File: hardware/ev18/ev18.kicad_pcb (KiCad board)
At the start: 4 copper layers, 112.3 x 90 mm, 234 parts, among them CN1 Conn_05x02_Female, CN2 PJ-242, J1 USB_C_Receptacle, J11 Conn_02x05_Counter_Clockwise, J2 Conn_01x02_Socket, J3 AudioJack4, J4 Conn_02x03_Odd_Even, J5 Conn_02x03_Odd_Even, J6 Conn_02x05_Counter_Clockwise, J7 Conn_02x05_Counter_Clockwise, J8 Conn_02x05_Counter_Clockwise, J9 Conn_02x05_Counter_Clockwise, Q1 2N7002, Q2 2N7002, Q3 2N7002, SW1 SW_SPDT, SW2 SW_Push, SW3 SW_Push, SW4 SW_Push, SW5 SW_Push, SW6 SW_Push, SW7 SW_Push, U1 BQ21040DBV, U10 STM32F405RGTx, U12 XC6227C301MR-G, U2 USBLC6-2P6, U3 STM32F072CBTx, U4 CH340C, U5 TPS63060, U6 WM8960CGEFL/RV, U7 ESP32-S3-WROOM-1, U8 M24C02-RMN6TP, U9 TPS2116DRL, Y1 Crystal_GND24

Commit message: address PR review
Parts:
- removed NT4: NetTie_2, NetTie:NetTie-2_SMD_Pad0.5mm
- TP31: moved to B.Cu
- moved TP31 42.4 mm to (74.4, 95.0), turned to 180 degrees
- moved R65 29.5 mm to (70.8, 95.9), turned to 90 degrees
- moved TP28 5.22 mm to (60.7, 42.8)
- moved TP3 1.10 mm to (64.1, 22.7)
- moved R11 0.62 mm to (72.1, 96.4)
- moved SW2 0.61 mm to (74.4, 95.0)
- moved R6 0.39 mm to (73.0, 98.8)
- moved R47 0.07 mm to (69.5, 96.4)
- moved C12 0.06 mm to (66.1, 102.1)
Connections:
- C12 pad 1: Net-(J2-Pin_2) -> /BQ_OUT
- R11 pad 1: Net-(J2-Pin_2) -> /BQ_OUT
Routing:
- net GNDA: track 118.4 -> 145.8 mm, vias 31 -> 36
- net Net-(J2-Pin_2): track 100.6 -> 89.0 mm, vias 6 -> 5
- net /BQ_OUT: track 1.47 -> 12.9 mm, vias 5 -> 7
- net VBUS: track 46.1 -> 49.7 mm
- net /MIC_N: track 23.2 -> 24.5 mm
- net Net-(D3-BK): track 19.6 -> 20.2 mm
- net VSYS: track 108.5 -> 109.0 mm
- net +3.0VA: track 12.9 -> 13.4 mm
- net Net-(D1-K): track 25.0 -> 24.4 mm
- net Net-(D1-A): track 3.91 -> 4.43 mm

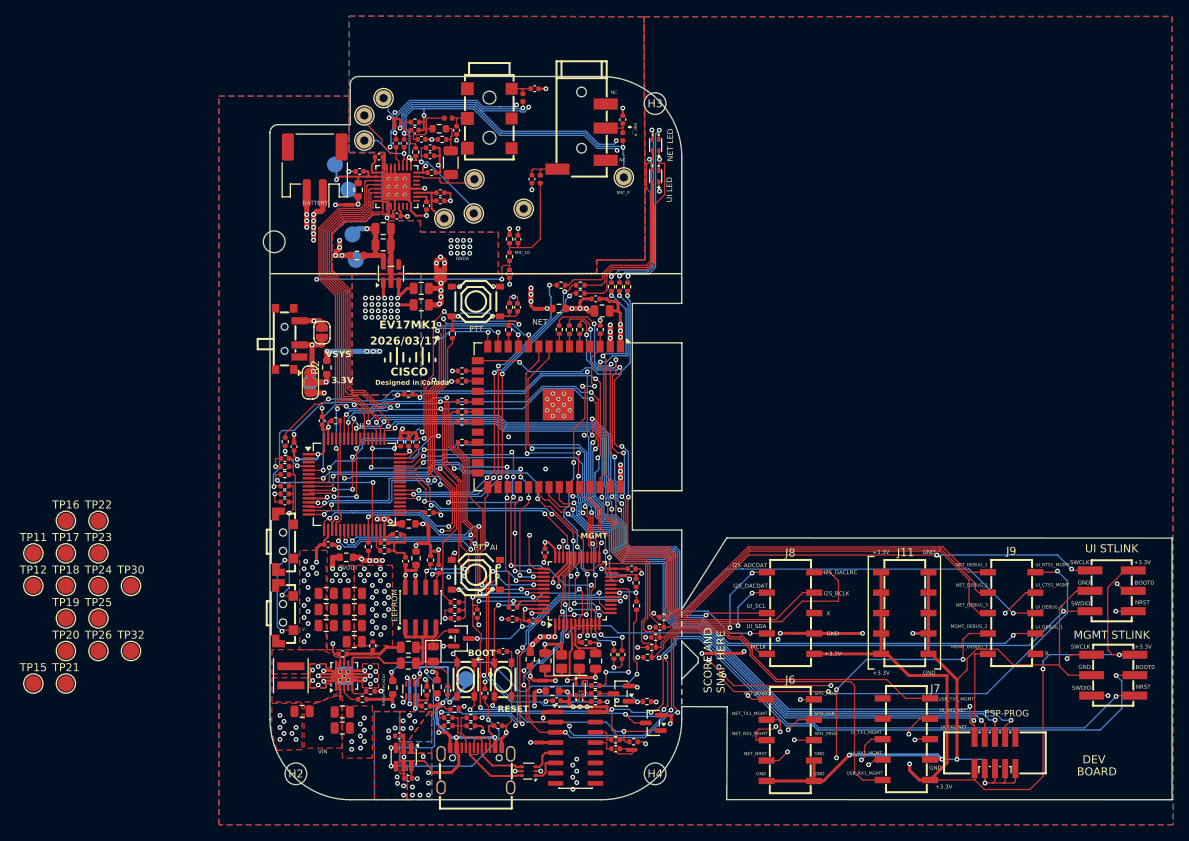
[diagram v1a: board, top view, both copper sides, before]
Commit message: Update side buttons, 3.5mm jack, and 2.5mm jack footprints to match their datasheets
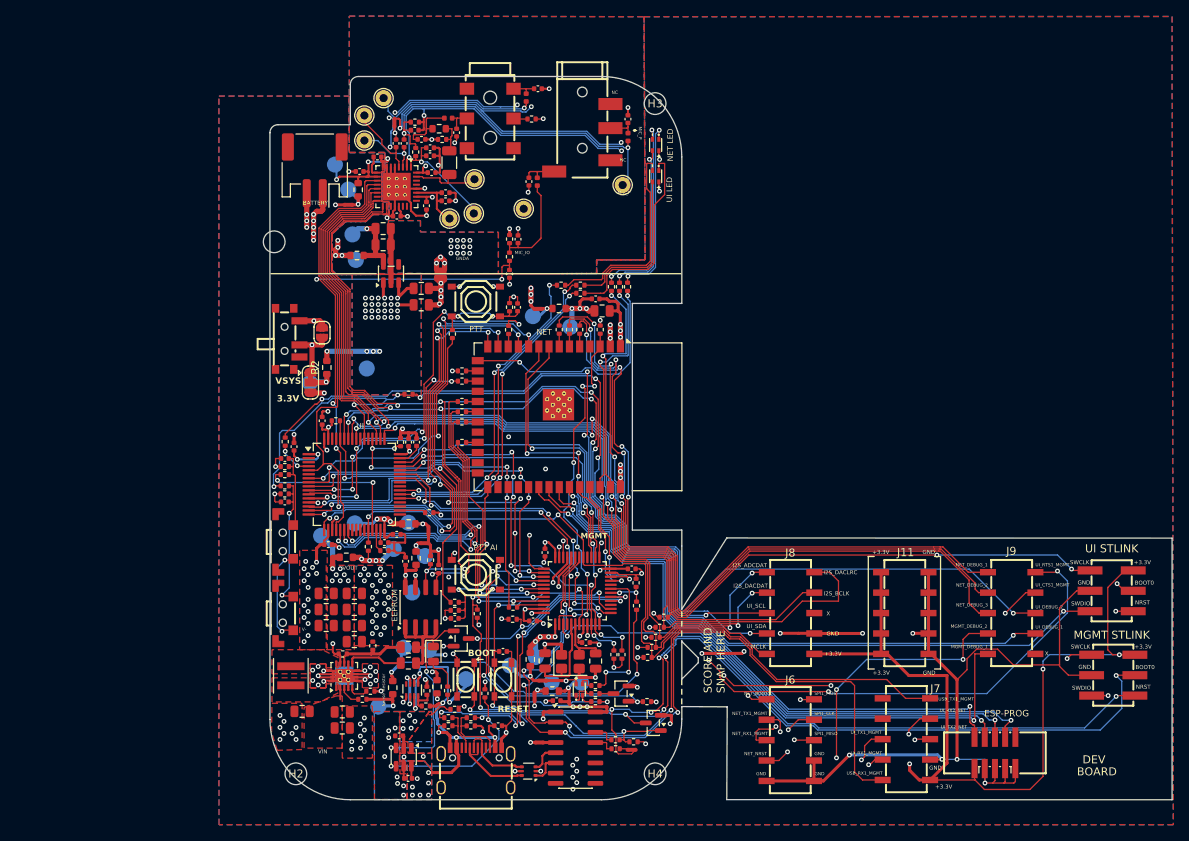
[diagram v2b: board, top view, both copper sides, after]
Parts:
- added R84: 1k0, Resistor_SMD:R_0402_1005Metric, F.Cu at (82.6, 25.3)
- TP11, TP12, TP15, TP16, TP17, TP18, TP19, TP20, TP21, TP22, TP23, TP24, TP25, TP26, TP30, TP32: moved to B.Cu
- moved TP17 68.8 mm to (87.4, 51.2), turned to 180 degrees
- moved TP18 67.1 mm to (82.7, 49.8), turned to 180 degrees
- moved TP21 64.1 mm to (88.7, 95.5), turned to 180 degrees
- moved TP22 59.9 mm to (85.1, 95.4), turned to 180 degrees
- moved TP19 58.7 mm to (83.1, 92.2), turned to 180 degrees
- moved TP20 55.3 mm to (79.9, 93.3), turned to 180 degrees
- moved TP11 48.8 mm to (69.3, 79.7), turned to 180 degrees
- moved TP12 47.2 mm to (67.7, 84.2), turned to 180 degrees
- moved TP15 44.7 mm to (60.6, 75.6), turned to 180 degrees
- moved TP16 42.6 mm to (67.2, 75.5), turned to 180 degrees
- moved TP30 39.9 mm to (62.0, 56.3), turned to 180 degrees
- moved TP25 38.2 mm to (66.6, 91.1), turned to 180 degrees
- moved TP32 37.1 mm to (69.8, 91.4), turned to 180 degrees
- moved TP24 37.0 mm to (65.4, 78.8), turned to 180 degrees
- moved TP26 35.5 mm to (63.5, 98.4), turned to 180 degrees
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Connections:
- CN2 pad 4: unconnected-(CN2-Pad4) -> Net-(CN2-Pad4)
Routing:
- net /MCLK: track 132.3 -> 127.0 mm, vias 5 -> 2
- net +3.3V_WM8960: track 10.5 -> 15.7 mm, vias 1 -> 3
- net /VOLUME-: track 30.4 -> 35.5 mm
- net Net-(J2-Pin_2): track 89.0 -> 93.8 mm, vias 5 -> 6
- net /BB_Vout: track 26.0 -> 30.7 mm
- net +3.3V: track 189.0 -> 192.5 mm, vias 28 -> 27
- net /MGMT_Sense: track 2.58 -> 5.64 mm
- net +3.3V_CH340C: track 15.1 -> 17.7 mm
- net +3.3V_EEPROM: track 4.93 -> 7.42 mm
- net +3.3V_Net: track 8.84 -> 11.2 mm
- net +3.3V_UI: track 26.2 -> 28.5 mm, vias 10 -> 11
- net GNDA: track 145.8 -> 148.1 mm, vias 36 -> 37
- net /CH340C_Sense: track 1.46 -> 3.76 mm
- net +3.3V_Mgmt: track 19.8 -> 22.0 mm
- net VSYS: track 109.0 -> 111.2 mm
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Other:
- board text added: "BB VOUT +"
- board text added: "BB VOUT -"
- board text added: "EV18"
- board text removed: "EV17MK1"

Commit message: Fixed ERC errors and warnings, and fixed update pcb warnings
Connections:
- U3 pad 32: /MGMT_UD_N -> unconnected-(U3-PA11-Pad32)
- U3 pad 33: /MGMT_UD_P -> unconnected-(U3-PA12-Pad33)
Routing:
- net unconnected-(U3-PA11-Pad32): track 0.00 -> 4.28 mm, vias 0 -> 1
- net /MGMT_UD_N: track 4.28 -> 0.00 mm, vias 1 -> 0
- net unconnected-(U3-PA12-Pad33): track 0.00 -> 3.86 mm, vias 0 -> 1
- net /MGMT_UD_P: track 3.86 -> 0.00 mm, vias 1 -> 0
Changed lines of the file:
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@@
 	(net 214 "/CH340C_Sense")
 	(net 215 "/MGMT_Sense")
-	(net 216 "/MGMT_UD_N")
-	(net 217 "/MGMT_UD_P")
+	(net 216 "unconnected-(U3-PA11-Pad32)")
+	(net 217 "unconnected-(U3-PA12-Pad33)")
 	(net 218 "/Jack_HP_L")
 	(net 219 "/Jack_MIC_N")
@@
 			(layers "F.Cu" "F.Mask" "F.Paste")
 			(roundrect_rratio 0.25)
-			(net 216 "/MGMT_UD_N")
+			(net 216 "unconnected-(U3-PA11-Pad32)")
 			(pinfunction "PA11")
-			(pintype "bidirectional")
+			(pintype "bidirectional+no_connect")
 		)
 		(pad "33" smd roundrect
@@
 			(layers "F.Cu" "F.Mask" "F.Paste")
 			(roundrect_rratio 0.25)
-			(net 217 "/MGMT_UD_P")
+			(net 217 "unconnected-(U3-PA12-Pad33)")
 			(pinfunction "PA12")
-			(pintype "bidirectional")
+			(pintype "bidirectional+no_connect")
 		)
 		(pad "34" smd roundrect
@@
 			)
 		)
+		(pad "" smd rect
+			(at -3.8 -0.78 90)
+			(size 1.1 0.93)
+			(layers "F.Cu" "F.Mask" "F.Paste")
+		)
+		(pad "" smd rect
+			(at -3.8 1.49 270)
+			(size 1.1 0.93)
+			(layers "F.Cu" "F.Mask" "F.Paste")
+		)
 		(pad "" np_thru_hole circle
 			(at -1.5 0.36 270)
@@
 			(layers "*.Cu" "*.Mask")
 		)
+		(pad "" smd rect
+			(at 3.8 -0.78 270)
+			(size 1.1 0.93)
+			(layers "F.Cu" "F.Mask" "F.Paste")
+		)
+		(pad "" smd rect
+			(at 3.8 1.49 270)
+			(size 1.1 0.93)
+			(layers "F.Cu" "F.Mask" "F.Paste")
+		)
 		(pad "1" smd rect
 			(at -2.25 -1.49 270)
@@
 			(pintype "passive+no_connect")
 		)
-		(pad "4" smd rect
-			(at 3.8 -0.78 270)
-			(size 1.1 0.93)
-			(layers "F.Cu" "F.Mask" "F.Paste")
-		)
-		(pad "5" smd rect
-			(at 3.8 1.49 270)
-			(size 1.1 0.93)
-			(layers "F.Cu" "F.Mask" "F.Paste")
-		)
-		(pad "6" smd rect
-			(at -3.8 1.49 270)
-			(size 1.1 0.93)
-			(layers "F.Cu" "F.Mask" "F.Paste")
-		)
-		(pad "7" smd rect
-			(at -3.8 -0.78 90)
-			(size 1.1 0.93)
-			(layers "F.Cu" "F.Mask" "F.Paste")
-		)
 		(embedded_fonts no)
 		(model "${KIPRJMOD}/../kicad_libraries/hactar_models.3dshapes/SW-SMD_MK-12C02-G020.wrl"
@@
 			)
 			(rotate
-				(xyz 0 0 0)
+				(xyz -0 -0 -0)
 			)
 		)
@@
 			(layers "F.Cu" "F.Mask" "F.Paste")
 			(net 7 "/MGMT_NRST")
+			(pinfunction "1")
 			(pintype "passive")
 		)
@@
 			(layers "F.Cu" "F.Mask" "F.Paste")
 			(net 7 "/MGMT_NRST")
+			(pinfunction "2")
 			(pintype "passive")
 		)
@@
 			(layers "F.Cu" "F.Mask" "F.Paste")
 			(net 3 "GND")
+			(pinfunction "3")
 			(pintype "passive")
 		)
@@
 			(layers "F.Cu" "F.Mask" "F.Paste")
 			(net 3 "GND")
+			(pinfunction "4")
 			(pintype "passive")
 		)
@@
 			(layers "F.Cu" "F.Mask" "F.Paste")
 			(net 1 "+3.3V")
+			(pinfunction "1")
 			(pintype "passive")
 		)
@@
 			(layers "F.Cu" "F.Mask" "F.Paste")
 			(net 1 "+3.3V")
+			(pinfunction "2")
 			(pintype "passive")
 		)
@@
 			(layers "F.Cu" "F.Mask" "F.Paste")
 			(net 74 "Net-(C47-Pad1)")
+			(pinfunction "3")
 			(pintype "passive")
 		)
@@
 			(layers "F.Cu" "F.Mask" "F.Paste")
 			(net 74 "Net-(C47-Pad1)")
+			(pinfunction "4")
 			(pintype "passive")
 		)
@@
 			(layers "F.Cu" "F.Mask" "F.Paste")
 			(net 1 "+3.3V")
+			(pinfunction "1")
 			(pintype "passive")
 		)
@@
 			(layers "F.Cu" "F.Mask" "F.Paste")
 			(net 1 "+3.3V")
+			(pinfunction "2")
 			(pintype "passive")
 		)
@@
 			(layers "F.Cu" "F.Mask" "F.Paste")
 			(net 73 "Net-(C46-Pad1)")
+			(pinfunction "3")
 			(pintype "passive")
 		)
@@
 			(layers "F.Cu" "F.Mask" "F.Paste")
 			(net 73 "Net-(C46-Pad1)")
+			(pinfunction "4")
 			(pintype "passive")
 		)
@@
 			)
 		)
+		(pad "" smd roundrect
+			(at -3.35 2.9 180)
+			(size 1.5 3.4)
+			(layers "F.Cu" "F.Mask" "F.Paste")
+			(roundrect_rratio 0.166667)
+		)
+		(pad "" smd roundrect
+			(at 3.35 2.9 180)
+			(size 1.5 3.4)
+			(layers "F.Cu" "F.Mask" "F.Paste")
+			(roundrect_rratio 0.166667)
+		)
 		(pad "1" smd roundrect
 			(at -1 -2.85 180)
@@
 			(pintype "passive")
 		)
-		(pad "MP" smd roundrect
-			(at -3.35 2.9 180)
-			(size 1.5 3.4)
-			(layers "F.Cu" "F.Mask" "F.Paste")
-			(roundrect_rratio 0.166667)
-		)
-		(pad "MP" smd roundrect
-			(at 3.35 2.9 180)
-			(size 1.5 3.4)
-			(layers "F.Cu" "F.Mask" "F.Paste")
-			(roundrect_rratio 0.166667)
-		)
 		(embedded_fonts no)
 		(model "${KIPRJMOD}/../kicad_libraries/hactar_models.3dshapes/CONN-SMD_P2.00_S2B-PH-SM4-TB-LF-SN.step"
@@
 			)
 			(rotate
-				(xyz 0 0 0)
+				(xyz -0 -0 -0)
 			)
 		)
@@
 			(layers "F.Cu" "F.Mask" "F.Paste")
 			(net 3 "GND")
+			(pinfunction "1")
 			(pintype "passive")
 		)
@@
 			(layers "F.Cu" "F.Mask" "F.Paste")
 			(net 3 "GND")
+			(pinfunction "2")
 			(pintype "passive")
 		)
@@
 			(layers "F.Cu" "F.Mask" "F.Paste")
 			(net 181 "Net-(Q3-G)")
+			(pinfunction "3")
 			(pintype "passive")
 		)
@@
 			(layers "F.Cu" "F.Mask" "F.Paste")
 			(net 181 "Net-(Q3-G)")
+			(pinfunction "4")
 			(pintype "passive")
 		)
@@
 			(roundrect_rratio 0.208333)
 			(net 3 "GND")
-			(pinfunction "2")
+			(pinfunction "G")
 			(pintype "passive")
 		)
@@
 			(roundrect_rratio 0.208333)
 			(net 3 "GND")
-			(pinfunction "4")
+			(pinfunction "G")
 			(pintype "passive")
 		)
